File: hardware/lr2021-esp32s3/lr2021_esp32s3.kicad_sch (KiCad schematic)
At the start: 84 parts, among them J1 USB-C, J2 5V IN, J3 3V3 IN, J4 GPIO, J5 SMA 915MHz, J6 SMA 2.4GHz, SW1 RESET, SW2 BOOT, U1 USBLC6-2SC6, U2 AP7361C-33E, U3 LM66100, U4 LM66100, U5 ESP32-S3-WROOM-1-N16R8, U6 LR2021IMLTRT, Y1 32MHz

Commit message: Route LR2021 + ESP32-S3 board; add fab outputs and build pipeline
- In2 becomes a +3V3 plane (L1 sig/RF, L2 GND, L3 3V3, L4 sig); every
  3V3/GND pad gets its own plane via
- Hand fanout of the LR2021 (crystal, NTC divider, SIMO loop, VBAT/VDCC/
  VPAX, SPI escape vias) and the duplicated USB-C pads; only DIO9 is used
  as IRQ (DIO7/8/11 freed to clear the QFN corner)
- Freerouting 1.9 routes the rest on L1/L4 (inner layers declared as power
  planes); single-layer vias removed, ~160 GND stitching vias added
- build.py: project -> schematic -> ERC -> PCB -> route (retried until DRC
  has no unconnected items) -> Gerbers/drill, JLCPCB BOM/CPL, PDFs, previews
- ERC: 0 errors (1 intentional LM66100 diode-OR warning)
  DRC with schematic parity: 0 errors, 0 unconnected, 0 parity issues

Co-Authored-By: Claude Opus 5.5 <noreply@anthropic.com>
Claude-Session: https://claude.ai/code/session_01GybN5CQfdUnddB4A81xgKu
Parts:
- H1, H2, H3, H4: now left out of the parts list
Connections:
- net LR_DIO11: no longer names the net of U6.7 (DIO11)
- net LR_DIO11: no longer U5.12 (IO8)
- net LR_DIO7: no longer names the net of U6.11 (DIO7)
- net LR_DIO7: no longer U5.17 (IO9)
- net LR_DIO8: no longer names the net of U6.10 (DIO8)
- net LR_DIO8: no longer U5.25 (IO48)
- no-connect marks 15 -> 21
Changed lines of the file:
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@@
 		)
 	)
-	(wire
-		(pts (xy 403.86 101.6) (xy 401.32 101.6))
-		(stroke (width 0) (type default))
-	)
-	(label "LR_DIO11"
-		(at 401.32 101.6 180)
-		(fields_autoplaced yes)
-		(effects
-			(font (size 1.27 1.27))
-			(justify right bottom)
-		)
-	)
-	(wire
-		(pts (xy 403.86 104.14) (xy 401.32 104.14))
-		(stroke (width 0) (type default))
-	)
-	(label "LR_DIO7"
-		(at 401.32 104.14 180)
-		(fields_autoplaced yes)
-		(effects
-			(font (size 1.27 1.27))
-			(justify right bottom)
-		)
-	)
+	(no_connect (at 403.86 101.6))
+	(no_connect (at 403.86 104.14))
 	(wire
 		(pts (xy 403.86 106.68) (xy 401.32 106.68))
@@
 		)
 	)
-	(wire
-		(pts (xy 434.34 121.92) (xy 436.88 121.92))
-		(stroke (width 0) (type default))
-	)
-	(label "LR_DIO8"
-		(at 436.88 121.92 0)
-		(fields_autoplaced yes)
-		(effects
-			(font (size 1.27 1.27))
-			(justify left bottom)
-		)
-	)
+	(no_connect (at 434.34 121.92))
 	(symbol
 		(lib_id "RF_Module:ESP32-S3-WROOM-1")
@@
 	(no_connect (at 170.18 299.72))
 	(no_connect (at 170.18 302.26))
-	(wire
-		(pts (xy 170.18 304.8) (xy 172.72 304.8))
-		(stroke (width 0) (type default))
-	)
-	(label "LR_DIO7"
-		(at 172.72 304.8 0)
-		(fields_autoplaced yes)
-		(effects
-			(font (size 1.27 1.27))
-			(justify left bottom)
-		)
-	)
-	(wire
-		(pts (xy 170.18 307.34) (xy 172.72 307.34))
-		(stroke (width 0) (type default))
-	)
-	(label "LR_DIO8"
-		(at 172.72 307.34 0)
-		(fields_autoplaced yes)
-		(effects
-			(font (size 1.27 1.27))
-			(justify left bottom)
-		)
-	)
+	(no_connect (at 170.18 304.8))
+	(no_connect (at 170.18 307.34))
 	(wire
 		(pts (xy 170.18 309.88) (xy 172.72 309.88))
@@
 	)
 	(no_connect (at 170.18 312.42))
-	(wire
-		(pts (xy 170.18 314.96) (xy 172.72 314.96))
-		(stroke (width 0) (type default))
-	)
-	(label "LR_DIO11"
-		(at 172.72 314.96 0)
-		(fields_autoplaced yes)
-		(effects
-			(font (size 1.27 1.27))
-			(justify left bottom)
-		)
-	)
+	(no_connect (at 170.18 314.96))
 	(wire
 		(pts (xy 143.51 274.32) (xy 143.51 271.78))
@@
 		(unit 1)
 		(exclude_from_sim no)
-		(in_bom yes)
+		(in_bom no)
 		(on_board yes)
 		(dnp no)
@@
 		(unit 1)
 		(exclude_from_sim no)
-		(in_bom yes)
+		(in_bom no)
 		(on_board yes)
 		(dnp no)
@@
 		(unit 1)
 		(exclude_from_sim no)
-		(in_bom yes)
+		(in_bom no)
 		(on_board yes)
 		(dnp no)
@@
 		(unit 1)
 		(exclude_from_sim no)
-		(in_bom yes)
+		(in_bom no)
 		(on_board yes)
 		(dnp no)

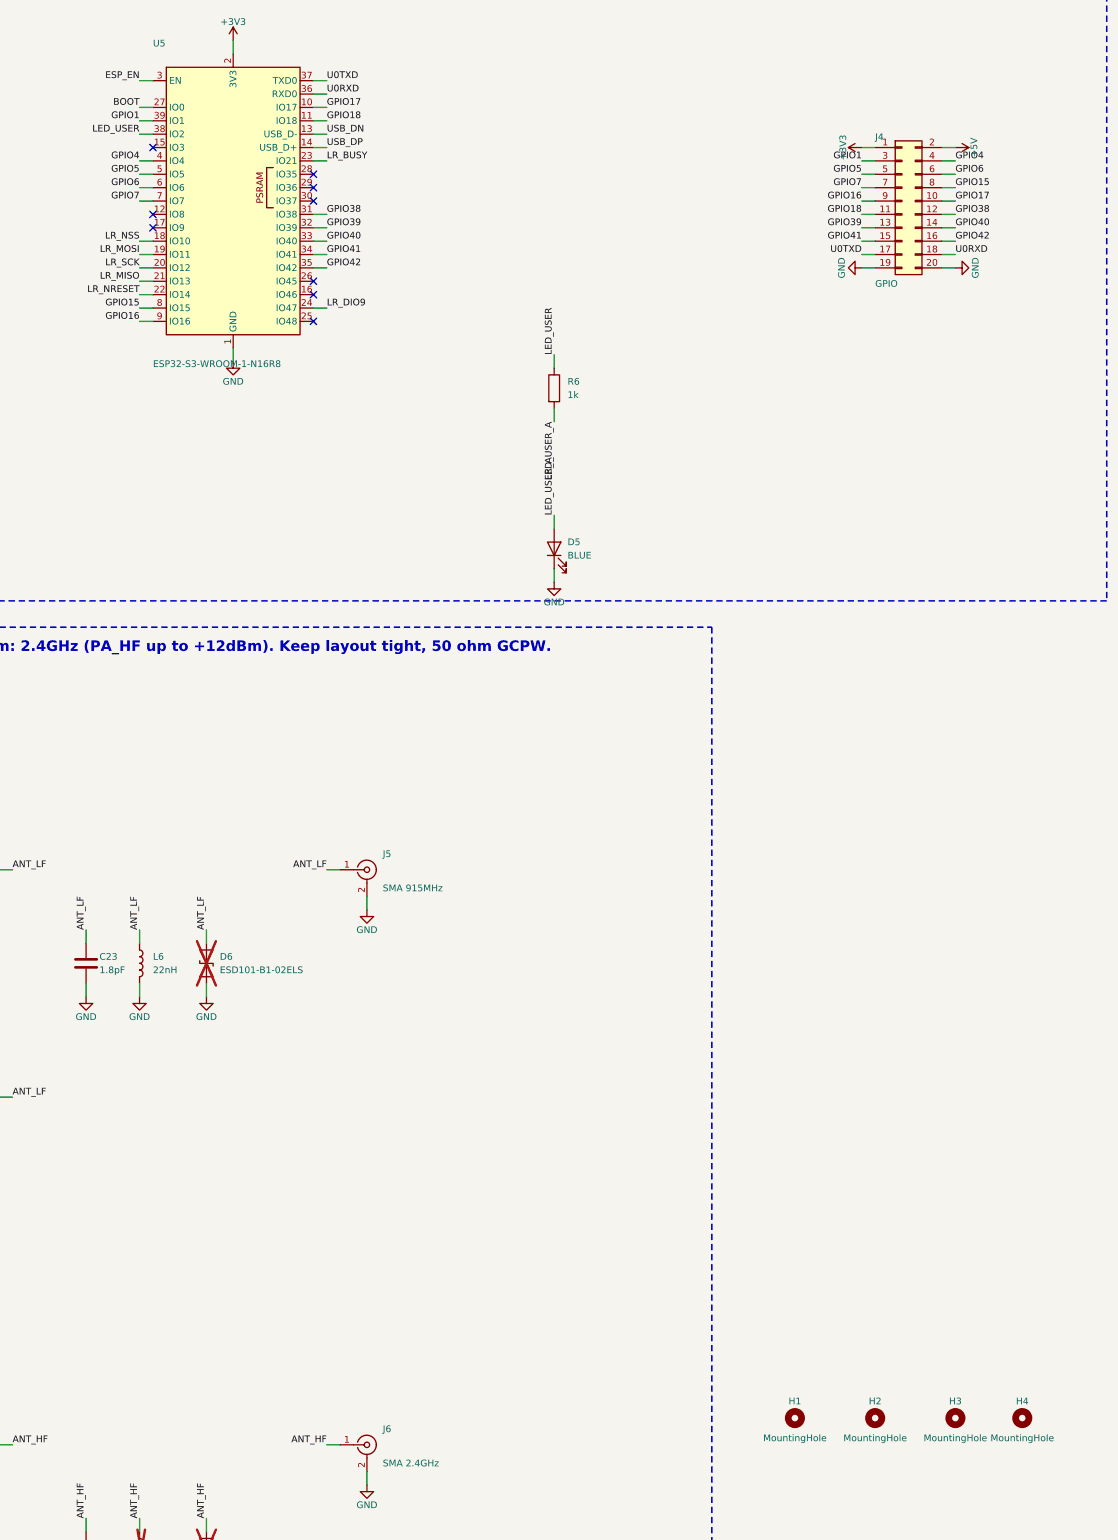
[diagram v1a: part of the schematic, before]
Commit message: Shrink the board from 90x65 mm to 64x52 mm
- Re-placed everything around the fixed constraints: ESP32 antenna at the
  top edge, LR2021 RF section and SMAs on the right, USB-C, terminals and
  GPIO header on the left/bottom edges
- Buttons rotated and moved next to the header; two M3 holes (right edge)
- GPIO header re-mapped to cut the routes crossing from the module's left
  side: now GPIO4-7, 9, 48, 38-42, 1 + UART, 3V3, 5V, 4x GND
  (GPIO15-18 no longer broken out)
- route.py keeps a 0.5 mm routing margin along the board edges
- ERC: 0 errors (intentional LM66100 OR warning); DRC with parity: 0 errors,
  0 unconnected; renders, drawings and fab outputs regenerated

Co-Authored-By: Claude Opus 5.5 <noreply@anthropic.com>
Claude-Session: https://claude.ai/code/session_01GybN5CQfdUnddB4A81xgKu
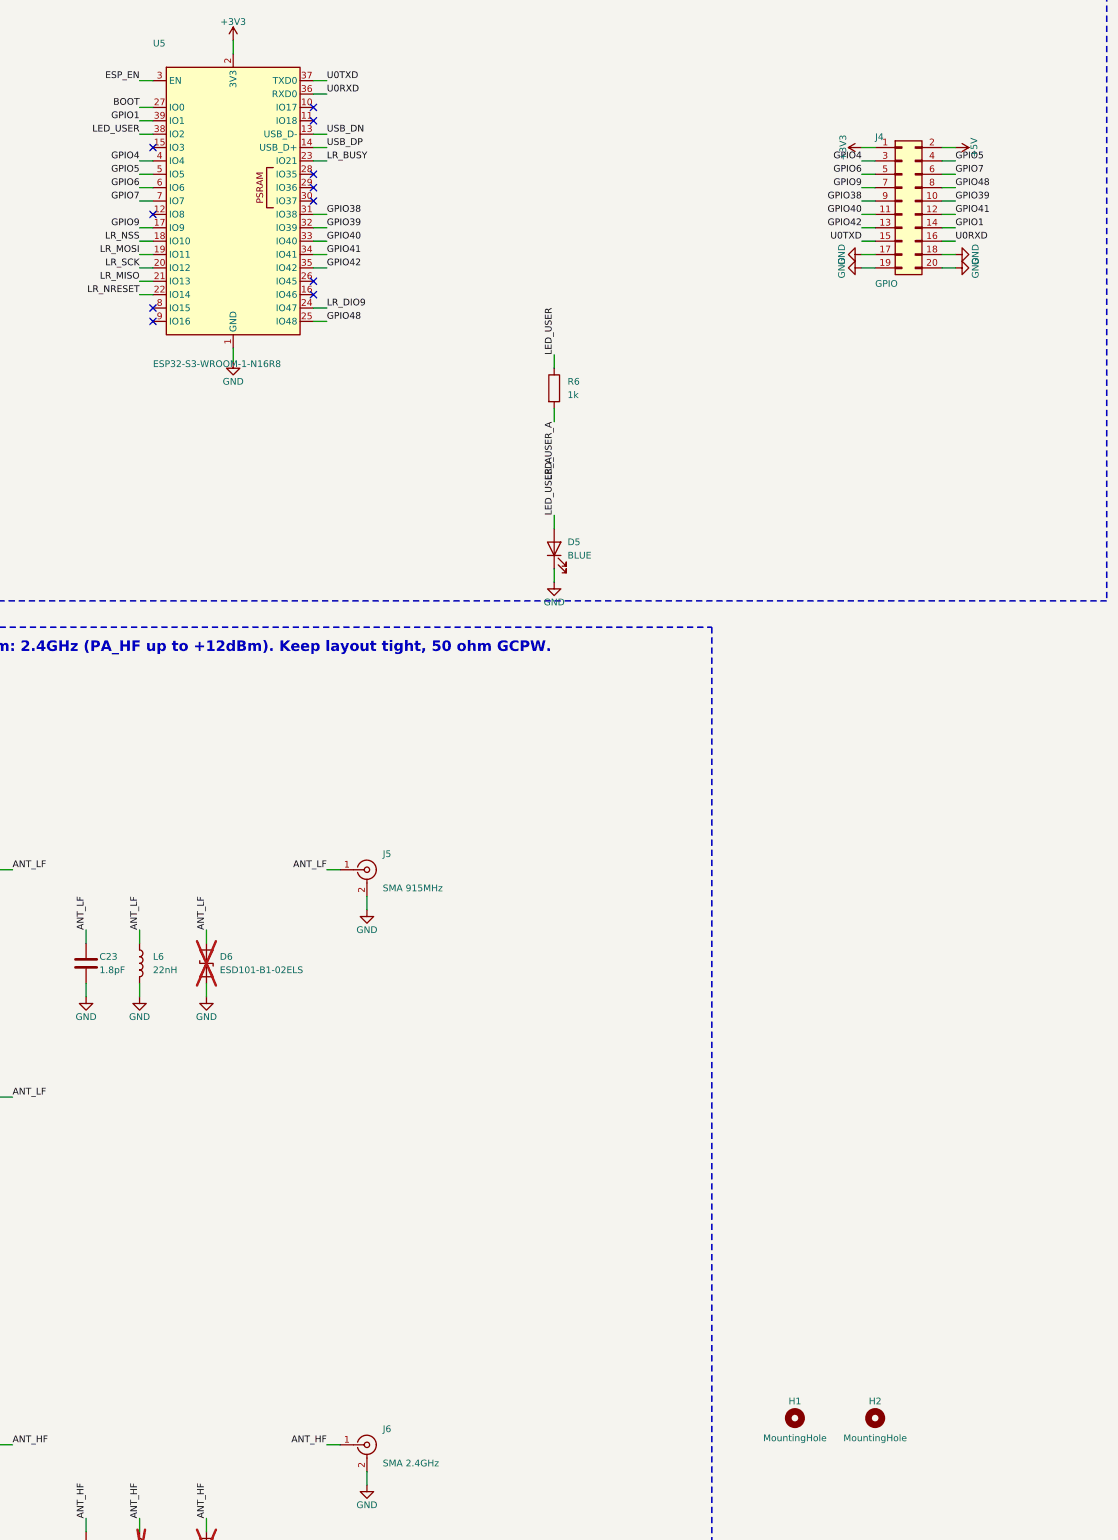
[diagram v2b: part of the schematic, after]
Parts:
- removed H3, H4: MountingHole, MountingHole:MountingHole_3.2mm_M3, symbol Mechanical:MountingHole
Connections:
- net GND: now also J4.17 (Pin_17), J4.18 (Pin_18)
- net GPIO1: now also J4.14 (Pin_14); no longer J4.3 (Pin_3)
- net GPIO38: now also J4.9 (Pin_9); no longer J4.12 (Pin_12)
- net GPIO39: now also J4.10 (Pin_10); no longer J4.13 (Pin_13)
- net GPIO4: now also J4.3 (Pin_3); no longer J4.4 (Pin_4)
- net GPIO40: now also J4.11 (Pin_11); no longer J4.14 (Pin_14)
- net GPIO41: now also J4.12 (Pin_12); no longer J4.15 (Pin_15)
- net GPIO42: now also J4.13 (Pin_13); no longer J4.16 (Pin_16)
- net GPIO5: now also J4.4 (Pin_4); no longer J4.5 (Pin_5)
- net GPIO6: now also J4.5 (Pin_5); no longer J4.6 (Pin_6)
- net GPIO7: now also J4.6 (Pin_6); no longer J4.7 (Pin_7)
- net U0RXD: now also J4.16 (Pin_16); no longer J4.18 (Pin_18)
- net U0TXD: now also J4.15 (Pin_15); no longer J4.17 (Pin_17)
- net GPIO9: now reaches U5.17 (IO9)
- net GPIO9: now also J4.7 (Pin_7)
- net GPIO48: now reaches U5.25 (IO48)
- net GPIO48: now also J4.8 (Pin_8)
- net GPIO15: no longer names the net of U5.8 (IO15)
- net GPIO15: no longer J4.8 (Pin_8)
- net GPIO16: no longer names the net of U5.9 (IO16)
- net GPIO16: no longer J4.9 (Pin_9)
- net GPIO17: no longer names the net of U5.10 (IO17)
- net GPIO17: no longer J4.10 (Pin_10)
- net GPIO18: no longer names the net of U5.11 (IO18)
- net GPIO18: no longer J4.11 (Pin_11)
- no-connect marks 21 -> 23

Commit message: Switch to ESP32-S3-WROOM-1U-N16R8 and shrink board to 62x47 mm (sources)
The U.FL module variant has no PCB antenna, so the antenna keepout is gone
and the module moves inside the board. Adds a STEP model for the module and
M2 mounting holes. Routed board and fab outputs follow.

Co-Authored-By: Claude Opus 5.5 <noreply@anthropic.com>
Claude-Session: https://claude.ai/code/session_01GybN5CQfdUnddB4A81xgKu
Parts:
- H1, H2: footprint MountingHole:MountingHole_3.2mm_M3 -> MountingHole:MountingHole_2.2mm_M2
- U5: value ESP32-S3-WROOM-1-N16R8 -> ESP32-S3-WROOM-1U-N16R8; footprint RF_Module:ESP32-S3-WROOM-1 -> RF_Module:ESP32-S3-WROOM-1U; LCSC C2913202 -> C3013946; MPN ESP32-S3-WROOM-1-N16R8 -> ESP32-S3-WROOM-1U-N16R8
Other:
- note added: "ESP32-S3-WROOM-1U-N16R8, radio unused (native USB on GPIO19/20; GPIO35-37 = PSRAM)"
- note removed: "ESP32-S3-WROOM-1-N16R8 (native USB on GPIO19/20; GPIO35-37 used by octal PSRAM)"
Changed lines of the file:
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@@
 			)
 		)
-		(property "Value" "ESP32-S3-WROOM-1-N16R8"
+		(property "Value" "ESP32-S3-WROOM-1U-N16R8"
 			(at 403.86 130 0)
 			(effects
@@
 			)
 		)
-		(property "Footprint" "RF_Module:ESP32-S3-WROOM-1"
+		(property "Footprint" "RF_Module:ESP32-S3-WROOM-1U"
 			(at 419.1 99.06 0)
 			(effects
@@
 			)
 		)
-		(property "MPN" "ESP32-S3-WROOM-1-N16R8"
+		(property "MPN" "ESP32-S3-WROOM-1U-N16R8"
 			(at 419.1 99.06 0)
 			(effects
@@
 			)
 		)
-		(property "LCSC" "C2913202"
+		(property "LCSC" "C3013946"
 			(at 419.1 99.06 0)
 			(effects
@@
 			)
 		)
-		(property "Footprint" "MountingHole:MountingHole_3.2mm_M3"
+		(property "Footprint" "MountingHole:MountingHole_2.2mm_M2"
 			(at 525.78 330.2 0)
 			(effects
@@
 			)
 		)
-		(property "Footprint" "MountingHole:MountingHole_3.2mm_M3"
+		(property "Footprint" "MountingHole:MountingHole_2.2mm_M2"
 			(at 541.02 330.2 0)
 			(effects
@@
 		)
 	)
-	(text "ESP32-S3-WROOM-1-N16R8 (native USB on GPIO19/20; GPIO35-37 used by octal PSRAM)"
+	(text "ESP32-S3-WROOM-1U-N16R8, radio unused (native USB on GPIO19/20; GPIO35-37 = PSRAM)"
 		(exclude_from_sim no)
 		(at 330 18 0)

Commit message: Fill in LCSC numbers for every BOM part; switch LEDs to AlInGaP
Stock checked in JLCPCB's parts search. The LR2021 (C49421489) is listed
but out of stock, so it needs Global Sourcing or consignment. Blue/InGaN
LEDs would barely light through 1k on 3.3V; USR is now red.

Co-Authored-By: Claude Opus 5.5 <noreply@anthropic.com>
Claude-Session: https://claude.ai/code/session_01GybN5CQfdUnddB4A81xgKu
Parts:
- C1, C3, C5: LCSC (none) -> C15850; MPN (none) -> CL21A106KAYNNNE
- C10, C11, C2, C4, C7: LCSC (none) -> C1525; MPN (none) -> CL05B104KO5NNNC
- C12: LCSC (none) -> C23733; MPN (none) -> CL05A475MP5NRNC
- C13, C14, C8: LCSC (none) -> C52923; MPN (none) -> CL05A105KA5NQNC
- C15, C16: LCSC (none) -> C107369; MPN (none) -> CL05A225KP5NSNC
- C17: LCSC (none) -> C1523; MPN (none) -> 0402B102K500NT
- C18, C26: LCSC (none) -> C60137; MPN (none) -> CC0402JRNPO9BN470
- C19: LCSC (none) -> C1555; MPN (none) -> 0402CG220J500NT
- C20: LCSC (none) -> C1855318; MPN (none) -> CQ0402BRNPO9BN7R5
- C21, C23: LCSC (none) -> C327209; MPN (none) -> CC0402BRNPO9BN1R8
- C22: LCSC (none) -> C505474; MPN (none) -> CC0402BRNPO9BN3R9
- C24, C32: LCSC (none) -> C1549; MPN (none) -> 0402CG180J500NT
- C25: LCSC (none) -> C325452; MPN (none) -> CC0402BRNPO9BN2R2
- C27: LCSC (none) -> C327291; MPN (none) -> CC0402BRNPO9BN6R8
- C28: LCSC (none) -> C326937; MPN (none) -> CC0402BRNPO9BN2R7
- C29: LCSC (none) -> C180259; MPN (none) -> RF15N1R1B500CT
- C30: LCSC (none) -> C327292; MPN (none) -> CC0402BRNPO9BN1R2
- C31: LCSC (none) -> C281756; MPN (none) -> CC0402BRNPO9BN2R0
- C6, C9: LCSC (none) -> C45783; MPN (none) -> CL21A226MAQNNNE
- D4: LCSC (none) -> C125094; MPN (none) -> LTST-C190KGKT
- D5: value BLUE -> RED; LCSC (none) -> C2286; MPN (none) -> KT-0603R
- J4: LCSC (none) -> C42372518; MPN (none) -> HX PZ2.54-2x10P ZZ
- J5, J6: LCSC (none) -> C5199907
- L10: LCSC (none) -> C778760; MPN (none) -> MWSD1005C1N6STM01
- L11: LCSC (none) -> C1332701; MPN (none) -> MHQ1005P1N1BT000
- L13, L5: LCSC (none) -> C113113; MPN (none) -> LQW15AN2N4B00D
- R1, R2: LCSC (none) -> C25905; MPN (none) -> 0402WGF5101TCE
- R3, R6: LCSC (none) -> C11702; MPN (none) -> 0402WGF1001TCE
- R4, R5, R7: LCSC (none) -> C25744; MPN (none) -> 0402WGF1002TCE
- R8: LCSC (none) -> C25750; MPN (none) -> 0402WGF1203TCE
- U6: LCSC (none) -> C49421489
- Y1: LCSC (none) -> C1986260; MPN (none) -> NX2016SA-32M-EXS00A-CS06465

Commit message: Pre-production fixes: JLC CPL corrections, LDO decoupling placement
- export_fab: per-LCSC rotation/offset corrections so JLCPCB places each part
  on our pads (the red LED would have gone in reversed; SOT-23-6, SC-70-6,
  SOT-223 and the SMA were rotated; THT parts and the ESP32/USB-C offset)
- check_cpl.py: overlays JLCPCB's EasyEDA footprints on our pads
- U2 rotated so its output cap sits 2.6 mm from OUT (was 9.1 mm); C2 is
  now a 1 uF input cap at IN, as the AP7361C datasheet asks
- TVS D3 moved next to D2

Co-Authored-By: Claude Opus 5.5 <noreply@anthropic.com>
Claude-Session: https://claude.ai/code/session_01GybN5CQfdUnddB4A81xgKu
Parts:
- C2: value 100nF -> 1uF; LCSC C1525 -> C52923; MPN CL05B104KO5NNNC -> CL05A105KA5NQNC
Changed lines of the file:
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@@
 			)
 		)
-		(property "Value" "100nF"
+		(property "Value" "1uF"
 			(at 190.5 62.23 0)
 			(effects
@@
 			)
 		)
-		(property "MPN" "CL05B104KO5NNNC"
+		(property "MPN" "CL05A105KA5NQNC"
 			(at 187.96 60.96 0)
 			(effects
@@
 			)
 		)
-		(property "LCSC" "C1525"
+		(property "LCSC" "C52923"
 			(at 187.96 60.96 0)
 			(effects

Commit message: Design review round 4: antenna ESD diodes and RF via fence
Full pre-production review with simulations (docs/design_review.md,
scripts in analysis/):
- ngspice power-path model: USB plug-in, LoRa TX + Wi-Fi droop,
  inrush and source switchover
- nodal RF model of both matching networks built from the netlist,
  and a graph comparison against Semtech's e788v01a reference
- thermal, current capacity and assembly spacing checks

Fixes:
- D6/D7 antenna ESD diodes are now fitted (DOWO PESD0402V12,
  C19626255, 0.05 pF, 12 V), as in the reference design
- add_rf_fence.py adds a 32-via GND fence along both antenna feeds
  after routing; build.py runs it and re-checks DRC

Fab files regenerated: Gerbers/drill (271 PTH), BOM and CPL.

Co-Authored-By: Claude Opus 5.5 <noreply@anthropic.com>
Claude-Session: https://claude.ai/code/session_01GybN5CQfdUnddB4A81xgKu
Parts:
- D6, D7: value ESD101-B1-02ELS -> PESD0402V12; LCSC (none) -> C19626255; MPN ESD101-B1-02ELS -> PESD0402V12; Spec Optional RF ESD, <=0.2pF, Vrwm>=5.5V -> Antenna ESD, 0.05pF, bidirectional, Vrwm 12V (Semtech ref p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; now fitted
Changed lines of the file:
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@@
 		(in_bom yes)
 		(on_board yes)
-		(dnp yes)
+		(dnp no)
 		(property "Reference" "D6"
 			(at 416.56 242.57 90)
@@
 			)
 		)
-		(property "Value" "ESD101-B1-02ELS"
+		(property "Value" "PESD0402V12"
 			(at 416.56 245.11 90)
 			(effects
@@
 			)
 		)
-		(property "MPN" "ESD101-B1-02ELS"
+		(property "MPN" "PESD0402V12"
 			(at 414.02 243.84 0)
 			(effects
@@
 			)
 		)
-		(property "Spec" "Optional RF ESD, <=0.2pF, Vrwm>=5.5V"
+		(property "LCSC" "C19626255"
+			(at 414.02 243.84 0)
+			(effects
+				(font (size 1.27 1.27))
+				(hide yes)
+			)
+		)
+		(property "Spec" "Antenna ESD, 0.05pF, bidirectional, Vrwm 12V (Semtech ref populates this)"
 			(at 414.02 243.84 0)
 			(effects
@@
 		(in_bom yes)
 		(on_board yes)
-		(dnp yes)
+		(dnp no)
 		(property "Reference" "D7"
 			(at 416.56 354.33 90)
@@
 			)
 		)
-		(property "Value" "ESD101-B1-02ELS"
+		(property "Value" "PESD0402V12"
 			(at 416.56 356.87 90)
 			(effects
@@
 			)
 		)
-		(property "MPN" "ESD101-B1-02ELS"
+		(property "MPN" "PESD0402V12"
 			(at 414.02 355.6 0)
 			(effects
@@
 			)
 		)
-		(property "Spec" "Optional RF ESD, <=0.2pF, Vrwm>=5.5V"
+		(property "LCSC" "C19626255"
 			(at 414.02 355.6 0)
 			(effects
+				(font (size 1.27 1.27))
+				(hide yes)
+			)
+		)
+		(property "Spec" "Antenna ESD, 0.05pF, bidirectional, Vrwm 12V (Semtech ref populates this)"
+			(at 414.02 355.6 0)
+			(effects
